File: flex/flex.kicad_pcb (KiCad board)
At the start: 2 copper layers, 68.2 x 125 mm, 11 parts, among them SW1 SW_Push, SW2 SW_Push, SW3 SW_Push

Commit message: started on firmware
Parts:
- SW2, SW3: moved to B.Cu
- moved H2 52.2 mm to (84.8, 143.9)
- moved SW3 17.4 mm to (130.0, 77.7), turned to 90 degrees
- moved SW2 9.34 mm to (130.0, 65.6), turned to 90 degrees
- moved H1 4.08 mm to (103.6, 36.1)
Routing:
- net /DISP_CS: track 114.8 -> 110.3 mm, vias 7 -> 5
- net /DISP_RESET: track 177.1 -> 175.5 mm
- net /DISP_SCK: track 131.5 -> 130.1 mm
- net /DISP_T_MOSI: track 114.6 -> 114.1 mm
- net GND: vias 56 -> 53
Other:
- board size 68.2 x 125 mm -> 62.2 x 125 mm

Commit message: added firmware and art
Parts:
- added G***: LOGO, LOGO, F.Cu at (104.3, 89.5)
- added G***: LOGO, LOGO, B.Cu at (103.9, 89.5)
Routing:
- net (no net): vias 15 -> 14

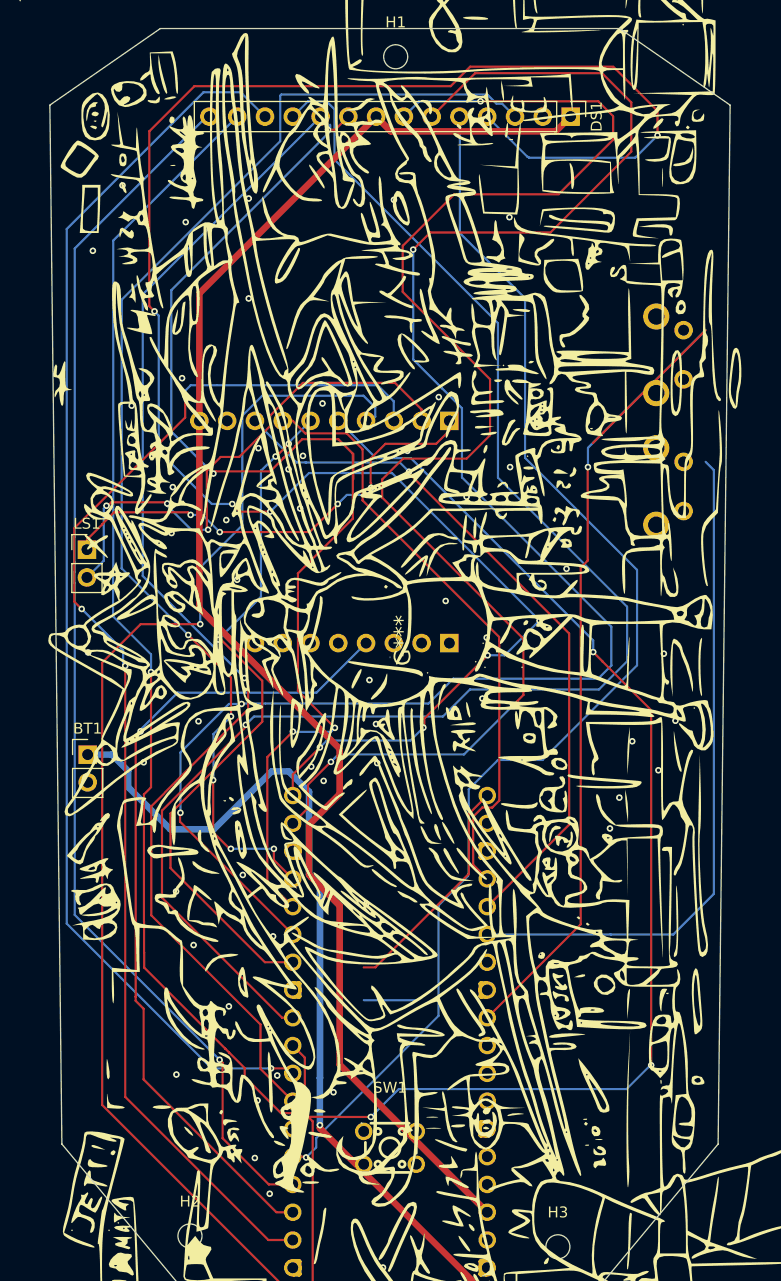
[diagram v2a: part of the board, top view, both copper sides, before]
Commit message: rendered and coded firmware
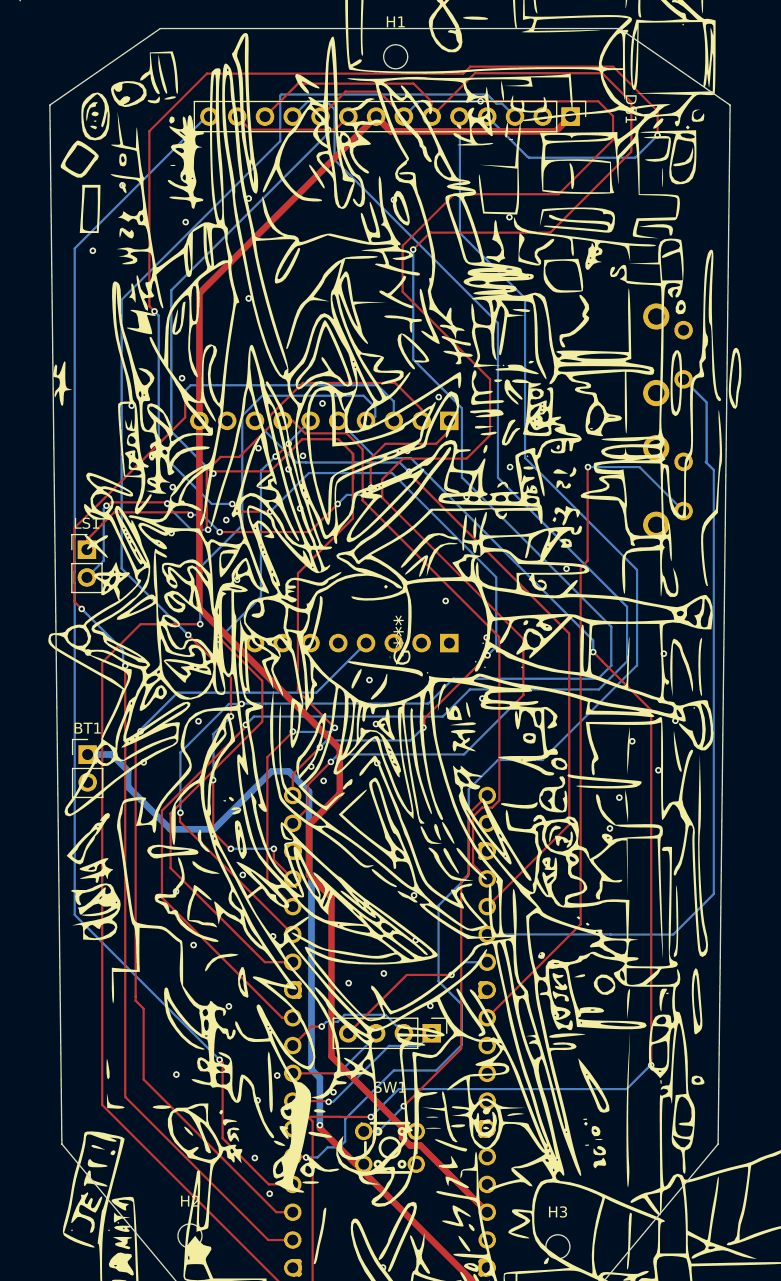
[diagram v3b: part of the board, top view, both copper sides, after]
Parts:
- DS1: footprint Connector_PinHeader_2.54mm:PinHeader_1x14_P2.54mm_Vertical -> LIB:Display
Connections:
- A1 pad 10: /DISP_T_MOSI -> /SD_MOSI
- A1 pad 11: /DISP_T_MISO -> /SD_MISO
- A1 pad 27: unconnected-(A1-GPIO21-Pad27) -> /SD_CS
- A1 pad 9: /DISP_T_CLK -> /SD_CLK
- DS1 pad 10: /DISP_T_CLK -> /DISP_SCK
- DS1 pad 12: /DISP_T_MOSI -> /DISP_MOSI
- DS1 pad 13: /DISP_T_MISO -> /DISP_MISO
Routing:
- net /DISP_T_MOSI: track 114.1 -> 0.00 mm, vias 1 -> 0
- net /DISP_T_MISO: track 111.8 -> 0.00 mm, vias 1 -> 0
- net /DISP_T_CLK: track 109.7 -> 0.00 mm, vias 1 -> 0
- net Net-(A1-GPIO22): track 85.7 -> 64.6 mm
- net /DISP_MOSI: track 158.2 -> 176.8 mm
- net /SD_CS: track 0.00 -> 15.4 mm, vias 0 -> 1
- net /SD_CLK: track 0.00 -> 15.3 mm, vias 0 -> 1
- net Net-(A1-GPIO16): track 21.0 -> 36.2 mm, vias 0 -> 1
- net /SD_MISO: track 0.00 -> 12.0 mm, vias 0 -> 1
- net /DISP_SCK: track 130.1 -> 139.6 mm
- net /SD_MOSI: track 0.00 -> 9.40 mm, vias 0 -> 1
- net Net-(A1-GPIO20): track 62.1 -> 70.6 mm
- net /DISP_MISO: track 109.4 -> 117.6 mm
- net /DISP_RS/DC: track 118.1 -> 123.3 mm
- net (no net): track 4.80 -> 0.00 mm
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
